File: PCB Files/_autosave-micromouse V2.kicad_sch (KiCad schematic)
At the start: 74 parts, among them J1 TOF1, J2 TOF1, J3 Conn_02x02_Counter_Clockwise, J4 BATT, J5 TOF1, J6 Conn_01x02_Pin, J7 Motor 1, J8 Motor 2, J9 USB-C, SW1 BOOT0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

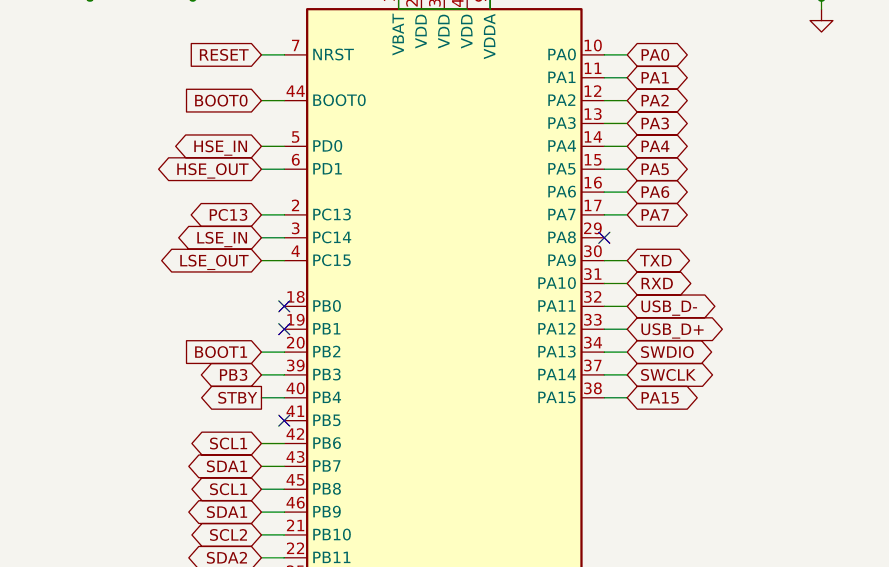
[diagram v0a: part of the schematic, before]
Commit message: Flipped TOF
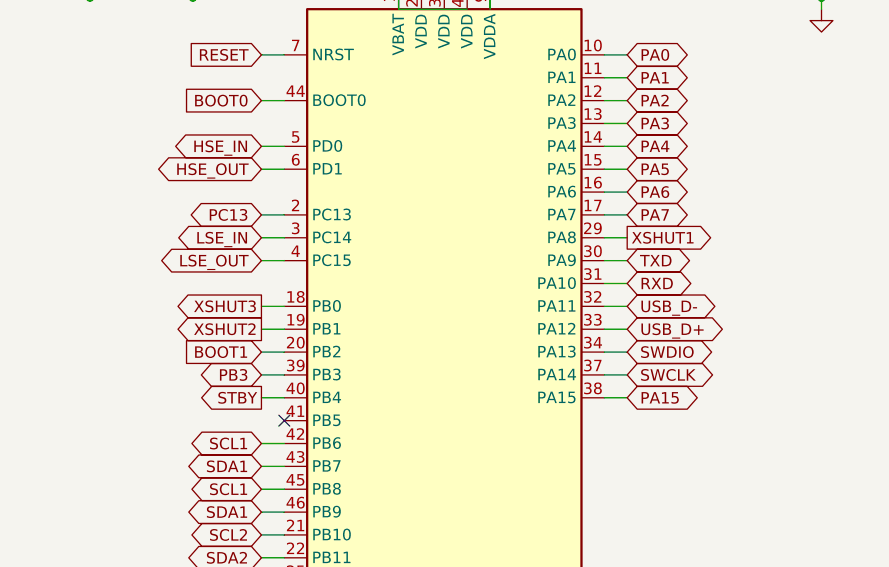
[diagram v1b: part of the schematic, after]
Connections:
- net XSHUT1: now also U4.29 (PA8)
- net XSHUT2: now also U4.19 (PB1)
- net XSHUT3: now also U4.18 (PB0)
- no-connect marks 15 -> 12
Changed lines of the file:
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@@
 	)
 	(no_connect
-		(at 68.58 77.47)
-	)
-	(no_connect
 		(at 68.58 87.63)
 	)
@@
 	)
 	(no_connect
-		(at 104.14 67.31)
-	)
-	(no_connect
 		(at 68.58 113.03)
 	)
@@
 	)
 	(no_connect
-		(at 68.58 74.93)
-	)
-	(no_connect
 		(at 381 85.09)
 	)
@@
 	(wire
 		(pts
+			(xy 66.04 77.47) (xy 68.58 77.47)
+		)
+		(stroke
+			(width 0)
+			(type default)
+		)
+	)
+	(wire
+		(pts
 			(xy 321.31 34.29) (xy 308.61 34.29)
 		)
@@
 	(wire
 		(pts
+			(xy 66.04 74.93) (xy 68.58 74.93)
+		)
+		(stroke
+			(width 0)
+			(type default)
+		)
+	)
+	(wire
+		(pts
 			(xy 181.61 163.83) (xy 181.61 166.37)
 		)
@@
 	(wire
 		(pts
+			(xy 106.68 67.31) (xy 104.14 67.31)
+		)
+		(stroke
+			(width 0)
+			(type default)
+		)
+	)
+	(wire
+		(pts
 			(xy 383.54 151.13) (xy 396.24 151.13)
 		)
@@
 		)
 	)
+	(global_label "XSHUT2"
+		(shape output)
+		(at 66.04 77.47 180)
+		(fields_autoplaced yes)
+		(effects
+			(font
+				(size 1.27 1.27)
+			)
+			(justify right)
+		)
+		(property "Intersheetrefs" "${INTERSHEET_REFS}"
+			(at 55.7977 77.47 0)
+			(effects
+				(font
+					(size 1.27 1.27)
+				)
+				(justify right)
+				(hide yes)
+			)
+		)
+	)
 	(global_label "SCL1"
 		(shape bidirectional)
@@
 		)
 	)
+	(global_label "XSHUT3"
+		(shape output)
+		(at 66.04 74.93 180)
+		(fields_autoplaced yes)
+		(effects
+			(font
+				(size 1.27 1.27)
+			)
+			(justify right)
+		)
+		(property "Intersheetrefs" "${INTERSHEET_REFS}"
+			(at 55.7977 74.93 0)
+			(effects
+				(font
+					(size 1.27 1.27)
+				)
+				(justify right)
+				(hide yes)
+			)
+		)
+	)
 	(global_label "HSE_OUT"
 		(shape bidirectional)
@@
 				(hide yes)
 			)
+		)
+	)
+	(global_label "XSHUT1"
+		(shape output)
+		(at 106.68 67.31 0)
+		(fields_autoplaced yes)
+		(effects
+			(font
+				(size 1.27 1.27)
+			)
+			(justify left)
+		)
+		(property "Intersheetrefs" "${INTERSHEET_REFS}"
+			(at 116.9223 67.31 0)
+			(effects
+				(font
+					(size 1.27 1.27)
+				)
+				(justify left)
+				(hide yes)
+			)
